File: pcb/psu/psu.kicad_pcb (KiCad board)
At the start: 2 copper layers, 40.6 x 33 mm, 4 parts, among them J1 VIN, J2 HEADER-1x01, J3 HEADER-1x01, J4 SIGNAL

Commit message: Cleanup
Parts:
- moved J3 0.63 mm to (154.9, 89.5)
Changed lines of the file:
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@@
   )
   (module conn-header:HDR-M-1x01 (layer F.Cu)
-    (at 154.305 89.535)
+    (at 154.94 89.535)
     (descr "Header - 100mil pitch - Male - Single Row, Vertical, 1 pos.")
     (fp_text reference J3 (at -1.524 -1.905) (layer F.SilkS)

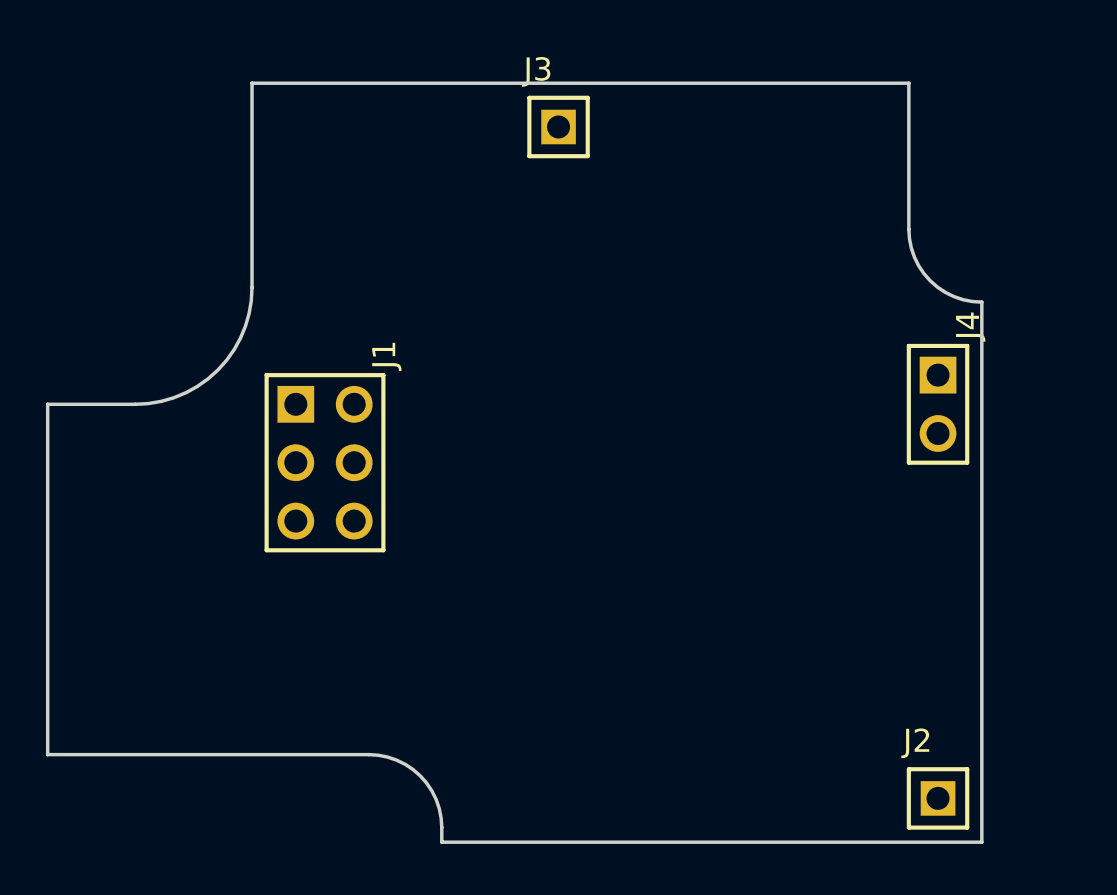
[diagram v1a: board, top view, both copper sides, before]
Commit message: Updated PCB design
+ Completed daughterboard PCB layout.
* Corrected soldermask clerance on front panel pcb.
- Removed input resistor on DIN for RGB lamp board.
* Modified PCB layout for PSU board.
* Updated gerber files.
* Updated schematics pdf, BOM.
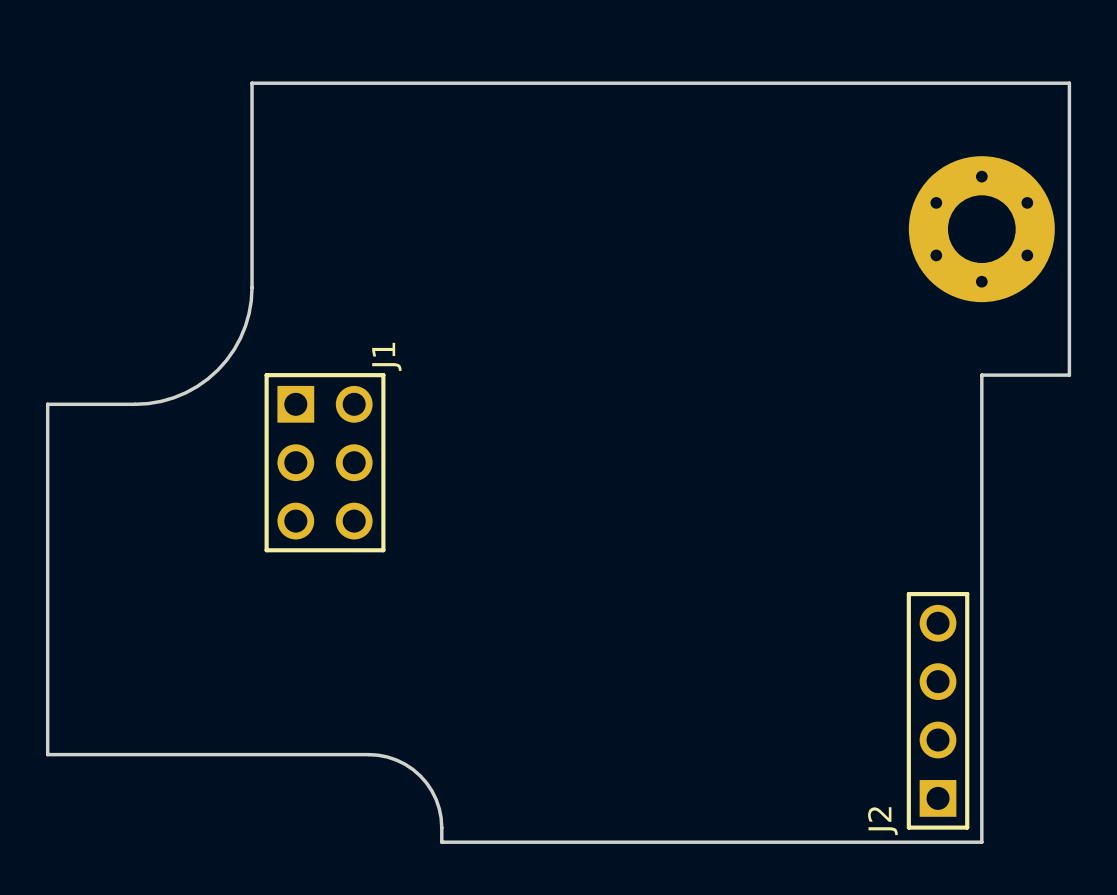
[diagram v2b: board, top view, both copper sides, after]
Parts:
- removed J4: SIGNAL, conn-header:HDR-M-1x02
- J2: value HEADER-1x01 -> HEADER-1x04; footprint conn-header:HDR-M-1x01 -> conn-header:HDR-M-1x04
- J3: footprint conn-header:HDR-M-1x01 -> conn-wire-pads:Hole-Screw-#4
- moved J3 18.9 mm to (173.4, 94.0)
- moved J2 3.81 mm to (171.4, 114.9), turned to 90 degrees
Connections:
- J2 pad 1: GND -> Net-(J2-Pad1)
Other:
- board size 40.6 x 33 mm -> 44.4 x 33 mm
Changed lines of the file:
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@@
     (tracks 0)
     (zones 0)
-    (modules 4)
-    (nets 7)
+    (modules 3)
+    (nets 9)
   )
   (page A4)
@@
   (net 1 "Net-(J1-Pad1)")
   (net 2 "Net-(J1-Pad2)")
-  (net 3 "Net-(J4-Pad1)")
-  (net 4 "Net-(J4-Pad2)")
-  (net 5 +5V)
-  (net 6 GND)
+  (net 3 +5V)
+  (net 4 GND)
+  (net 5 "Net-(J2-Pad1)")
+  (net 6 "Net-(J2-Pad2)")
+  (net 7 "Net-(J2-Pad3)")
+  (net 8 "Net-(J2-Pad4)")
   (net_class Default "This is the default net class."
     (clearance 0.2)
@@
     (add_net "Net-(J1-Pad1)")
     (add_net "Net-(J1-Pad2)")
-    (add_net "Net-(J4-Pad1)")
-    (add_net "Net-(J4-Pad2)")
+    (add_net "Net-(J2-Pad1)")
+    (add_net "Net-(J2-Pad2)")
+    (add_net "Net-(J2-Pad3)")
+    (add_net "Net-(J2-Pad4)")
   )
   (module conn-header:HDR-M-2x03 (layer F.Cu)
@@
       (net 2 "Net-(J1-Pad2)"))
     (pad 3 thru_hole circle (at 0 1.27 270) (size 1.6 1.6) (drill 1) (layers *.Cu *.Mask)
-      (net 5 +5V))
+      (net 3 +5V))
     (pad 4 thru_hole circle (at 0 -1.27 270) (size 1.6 1.6) (drill 1) (layers *.Cu *.Mask)
-      (net 5 +5V))
+      (net 3 +5V))
     (pad 5 thru_hole circle (at 2.54 1.27 270) (size 1.6 1.6) (drill 1) (layers *.Cu *.Mask)
-      (net 6 GND))
+      (net 4 GND))
     (pad 6 thru_hole circle (at 2.54 -1.27 270) (size 1.6 1.6) (drill 1) (layers *.Cu *.Mask)
-      (net 6 GND))
+      (net 4 GND))
     (model conn-header.pretty/HDR-M-2x03.wrl
       (at (xyz 0 0 0))
@@
     )
   )
-  (module conn-header:HDR-M-1x01 (layer F.Cu)
-    (at 171.45 118.745)
-    (descr "Header - 100mil pitch - Male - Single Row, Vertical, 1 pos.")
-    (fp_text reference J2 (at -1.524 -1.905) (layer F.SilkS)
+  (module conn-header:HDR-M-1x04 (layer F.Cu)
+    (at 171.45 114.935 90)
+    (descr "Header - 100mil pitch - Male - Single Row, Vertical, 4 pos.")
+    (fp_text reference J2 (at -5.334 -1.905 90) (layer F.SilkS)
       (effects (font (size 1 1) (thickness 0.18)) (justify left bottom))
     )
-    (fp_text value HEADER-1x01 (at 0 2.667) (layer F.SilkS) hide
-      (effects (font (size 1 1) (thickness 0.18)))
-    )
-    (fp_line (start -1.778 -1.778) (end 1.778 -1.778) (layer F.CrtYd) (width 0.05))
-    (fp_line (start 1.778 -1.778) (end 1.778 1.778) (layer F.CrtYd) (width 0.05))
-    (fp_line (start 1.778 1.778) (end -1.778 1.778) (layer F.CrtYd) (width 0.05))
-    (fp_line (start -1.778 1.778) (end -1.778 -1.778) (layer F.CrtYd) (width 0.05))
-    (fp_line (start -1.27 -1.27) (end 1.27 -1.27) (layer F.SilkS) (width 0.18))
-    (fp_line (start 1.27 -1.27) (end 1.27 1.27) (layer F.SilkS) (width 0.18))
-    (fp_line (start 1.27 1.27) (end -1.27 1.27) (layer F.SilkS) (width 0.18))
-    (fp_line (start -1.27 1.27) (end -1.27 -1.27) (layer F.SilkS) (width 0.18))
-    (pad 1 thru_hole rect (at 0 0) (size 1.508 1.508) (drill 1) (layers *.Cu *.Mask)
-      (net 6 GND))
-    (model conn-header.pretty/HDR-M-1x01.wrl
+    (fp_text value HEADER-1x04 (at 0 2.667 90) (layer F.SilkS) hide
+      (effects (font (size 1 1) (thickness 0.18)))
+    )
+    (fp_line (start -5.588 -1.778) (end 5.588 -1.778) (layer F.CrtYd) (width 0.05))
+    (fp_line (start 5.588 -1.778) (end 5.588 1.778) (layer F.CrtYd) (width 0.05))
+    (fp_line (start 5.588 1.778) (end -5.588 1.778) (layer F.CrtYd) (width 0.05))
+    (fp_line (start -5.588 1.778) (end -5.588 -1.778) (layer F.CrtYd) (width 0.05))
+    (fp_line (start -5.08 -1.27) (end 5.08 -1.27) (layer F.SilkS) (width 0.18))
+    (fp_line (start 5.08 -1.27) (end 5.08 1.27) (layer F.SilkS) (width 0.18))
+    (fp_line (start 5.08 1.27) (end -5.08 1.27) (layer F.SilkS) (width 0.18))
+    (fp_line (start -5.08 1.27) (end -5.08 -1.27) (layer F.SilkS) (width 0.18))
+    (pad 1 thru_hole rect (at -3.81 0 90) (size 1.6 1.6) (drill 1) (layers *.Cu *.Mask)
+      (net 5 "Net-(J2-Pad1)"))
+    (pad 2 thru_hole circle (at -1.27 0 90) (size 1.6 1.6) (drill 1) (layers *.Cu *.Mask)
+      (net 6 "Net-(J2-Pad2)"))
+    (pad 3 thru_hole circle (at 1.27 0 90) (size 1.6 1.6) (drill 1) (layers *.Cu *.Mask)
+      (net 7 "Net-(J2-Pad3)"))
+    (pad 4 thru_hole circle (at 3.81 0 90) (size 1.6 1.6) (drill 1) (layers *.Cu *.Mask)
+      (net 8 "Net-(J2-Pad4)"))
+    (model conn-header.pretty/HDR-M-1x04.wrl
       (at (xyz 0 0 0))
       (scale (xyz 1 1 1))
@@
     )
   )
-  (module conn-header:HDR-M-1x01 (layer F.Cu)
-    (at 154.94 89.535)
-    (descr "Header - 100mil pitch - Male - Single Row, Vertical, 1 pos.")
-    (fp_text reference J3 (at -1.524 -1.905) (layer F.SilkS)
-      (effects (font (size 1 1) (thickness 0.18)) (justify left bottom))
-    )
-    (fp_text value HEADER-1x01 (at 0 2.667) (layer F.SilkS) hide
-      (effects (font (size 1 1) (thickness 0.18)))
-    )
-    (fp_line (start -1.27 1.27) (end -1.27 -1.27) (layer F.SilkS) (width 0.18))
-    (fp_line (start 1.27 1.27) (end -1.27 1.27) (layer F.SilkS) (width 0.18))
-    (fp_line (start 1.27 -1.27) (end 1.27 1.27) (layer F.SilkS) (width 0.18))
-    (fp_line (start -1.27 -1.27) (end 1.27 -1.27) (layer F.SilkS) (width 0.18))
-    (fp_line (start -1.778 1.778) (end -1.778 -1.778) (layer F.CrtYd) (width 0.05))
-    (fp_line (start 1.778 1.778) (end -1.778 1.778) (layer F.CrtYd) (width 0.05))
-    (fp_line (start 1.778 -1.778) (end 1.778 1.778) (layer F.CrtYd) (width 0.05))
-    (fp_line (start -1.778 -1.778) (end 1.778 -1.778) (layer F.CrtYd) (width 0.05))
-    (pad 1 thru_hole rect (at 0 0) (size 1.508 1.508) (drill 1) (layers *.Cu *.Mask)
-      (net 6 GND))
-    (model conn-header.pretty/HDR-M-1x01.wrl
-      (at (xyz 0 0 0))
-      (scale (xyz 1 1 1))
-      (rotate (xyz 0 0 0))
-    )
-  )
-  (module conn-header:HDR-M-1x02 (layer F.Cu)
-    (at 171.45 101.6 270)
-    (descr "Header - 100mil pitch - Male - Single Row, Vertical, 2 pos.")
-    (fp_text reference J4 (at -2.794 -1.905 270) (layer F.SilkS)
-      (effects (font (size 1 1) (thickness 0.18)) (justify left bottom))
-    )
-    (fp_text value SIGNAL (at 0 2.667 270) (layer F.SilkS) hide
-      (effects (font (size 1 1) (thickness 0.18)))
-    )
-    (fp_line (start -3.048 -1.778) (end 3.048 -1.778) (layer F.CrtYd) (width 0.05))
-    (fp_line (start 3.048 -1.778) (end 3.048 1.778) (layer F.CrtYd) (width 0.05))
-    (fp_line (start 3.048 1.778) (end -3.048 1.778) (layer F.CrtYd) (width 0.05))
-    (fp_line (start -3.048 1.778) (end -3.048 -1.778) (layer F.CrtYd) (width 0.05))
-    (fp_line (start -2.54 -1.27) (end 2.54 -1.27) (layer F.SilkS) (width 0.18))
-    (fp_line (start 2.54 -1.27) (end 2.54 1.27) (layer F.SilkS) (width 0.18))
-    (fp_line (start 2.54 1.27) (end -2.54 1.27) (layer F.SilkS) (width 0.18))
-    (fp_line (start -2.54 1.27) (end -2.54 -1.27) (layer F.SilkS) (width 0.18))
-    (pad 1 thru_hole rect (at -1.27 0 270) (size 1.6 1.6) (drill 1) (layers *.Cu *.Mask)
-      (net 3 "Net-(J4-Pad1)"))
-    (pad 2 thru_hole circle (at 1.27 0 270) (size 1.6 1.6) (drill 1) (layers *.Cu *.Mask)
-      (net 4 "Net-(J4-Pad2)"))
-    (model conn-header.pretty/HDR-M-1x02.wrl
-      (at (xyz 0 0 0))
-      (scale (xyz 1 1 1))
-      (rotate (xyz 0 0 0))
-    )
-  )
+  (module conn-wire-pads:Hole-Screw-#4 locked (layer F.Cu)
+    (at 173.355 93.98)
+    (descr "Mounting Hole - Screw #4 - w/ Pads And Via")
+    (attr virtual)
+    (fp_text reference J3 (at 0 -4.6) (layer F.SilkS) hide
+      (effects (font (size 1 1) (thickness 0.18)))
+    )
+    (fp_text value HEADER-1x01 (at 0 4.7) (layer F.Fab) hide
+      (effects (font (size 1 1) (thickness 0.18)))
+    )
+    (fp_circle (center 0 0) (end 3.81 0) (layer F.CrtYd) (width 0.05))
+    (pad P thru_hole circle (at 1.979734 -1.143 300) (size 1.016 1.016) (drill 0.508) (layers *.Cu)
+      (zone_connect 2))
+    (pad P thru_hole circle (at 1.979734 1.143 240) (size 1.016 1.016) (drill 0.508) (layers *.Cu)
+      (zone_connect 2))
+    (pad P thru_hole circle (at 0 2.286 180) (size 1.016 1.016) (drill 0.508) (layers *.Cu)
+      (zone_connect 2))
+    (pad P thru_hole circle (at -1.979734 1.143 120) (size 1.016 1.016) (drill 0.508) (layers *.Cu)
+      (zone_connect 2))
+    (pad P thru_hole circle (at -1.979734 -1.143 60) (size 1.016 1.016) (drill 0.508) (layers *.Cu)
+      (zone_connect 2))
+    (pad P thru_hole circle (at 0 -2.286) (size 1.016 1.016) (drill 0.508) (layers *.Cu)
+      (zone_connect 2))
+    (pad P thru_hole circle (at 0 0) (size 6.35 6.35) (drill 2.9464) (layers *.Cu *.Mask)
+      (clearance 0.635) (zone_connect 2))
+  )
+  (gr_line (start 177.165 100.33) (end 177.165 87.63) (layer Edge.Cuts) (width 0.15))
+  (gr_line (start 173.355 100.33) (end 177.165 100.33) (layer Edge.Cuts) (width 0.15))
   (gr_arc (start 146.685 120.015) (end 149.86 120.015) (angle -90) (layer Edge.Cuts) (width 0.15))
   (gr_line (start 132.715 101.6) (end 132.715 116.84) (layer Edge.Cuts) (width 0.15))
@@
   (gr_arc (start 136.525 96.52) (end 136.525 101.6) (angle -90) (layer Edge.Cuts) (width 0.15))
   (gr_line (start 141.605 87.63) (end 141.605 96.52) (layer Edge.Cuts) (width 0.15))
-  (gr_line (start 170.18 87.63) (end 141.605 87.63) (layer Edge.Cuts) (width 0.15))
-  (gr_line (start 170.18 93.98) (end 170.18 87.63) (layer Edge.Cuts) (width 0.15))
-  (gr_arc (start 173.355 93.98) (end 170.18 93.98) (angle -90) (layer Edge.Cuts) (width 0.15))
-  (gr_line (start 173.355 120.65) (end 173.355 97.155) (layer Edge.Cuts) (width 0.15))
+  (gr_line (start 177.165 87.63) (end 141.605 87.63) (layer Edge.Cuts) (width 0.15))
+  (gr_line (start 173.355 120.65) (end 173.355 100.33) (layer Edge.Cuts) (width 0.15))
   (gr_line (start 149.86 120.65) (end 173.355 120.65) (layer Edge.Cuts) (width 0.15))
   (gr_line (start 149.86 120.015) (end 149.86 120.65) (layer Edge.Cuts) (width 0.15))
